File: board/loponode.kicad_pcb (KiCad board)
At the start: 2 copper layers, 44.4 x 25.9 mm, 25 parts, among them J1 DEBUG, J2 POWER_IN, J3 DBG_UART, J4 Conn_01x14, U1 TPS61322, U2 STM32L073CBTx, U3 NRF24L01+, Y1 8MHz

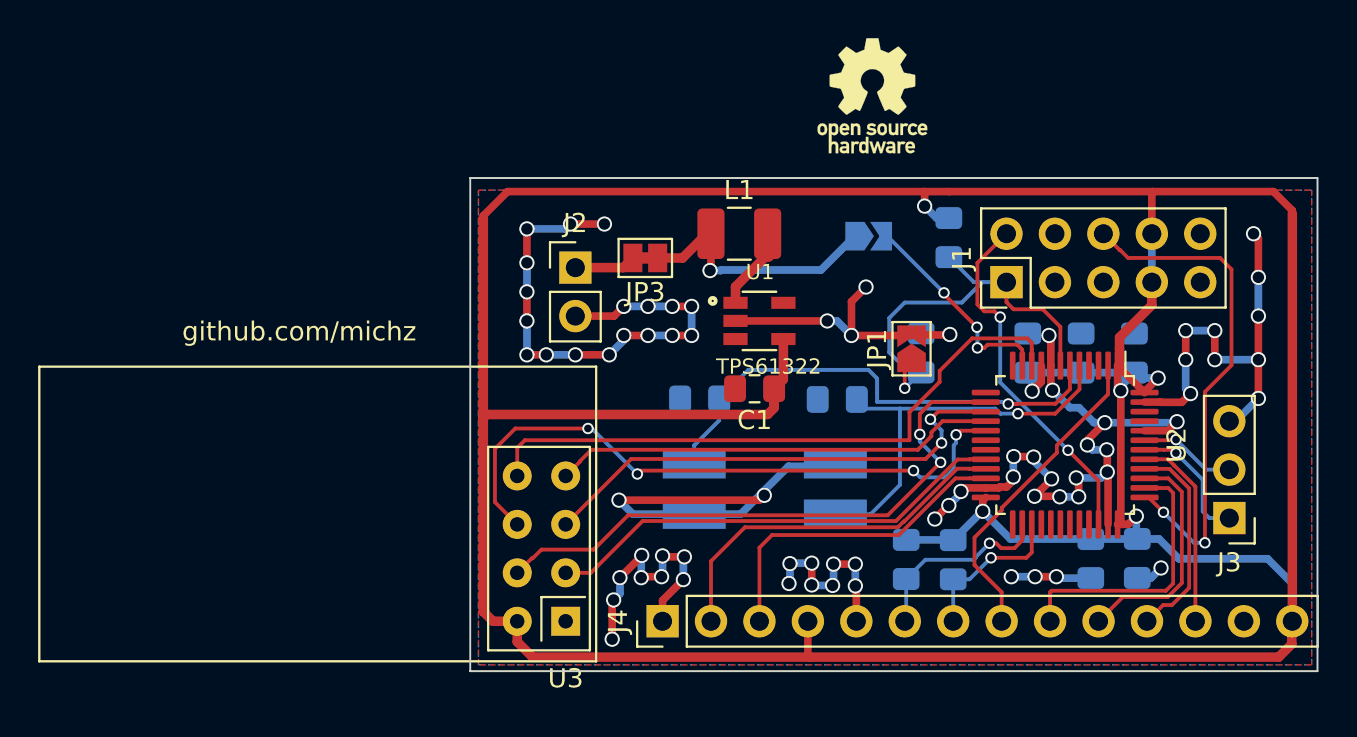
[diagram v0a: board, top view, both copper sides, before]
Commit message: move open hardware marking
+ fix some absolute path manually
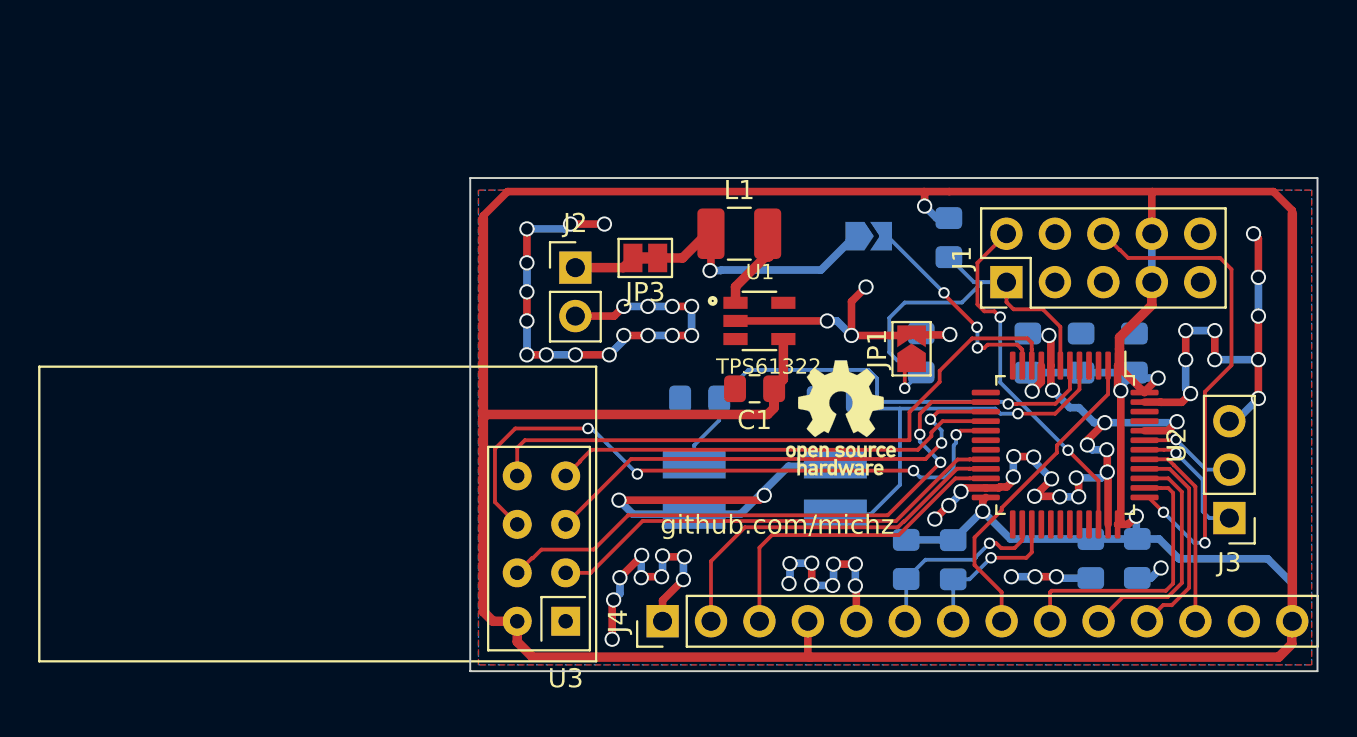
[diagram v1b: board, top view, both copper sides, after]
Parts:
- moved REF** 17.0 mm to (131.3, 134.1)
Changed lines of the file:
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@@
   )
   (module Symbol:OSHW-Logo_5.7x6mm_SilkScreen (layer F.Cu)
-    (at 132.9182 117.221)
+    (at 131.2672 134.112)
     (descr "Open Source Hardware Logo")
     (tags "Logo OSHW")
@@
   (gr_line (start 156.2608 147.3962) (end 156.2608 121.539) (layer Edge.Cuts) (width 0.1))
   (gr_line (start 111.8362 147.3962) (end 156.2608 147.3962) (layer Edge.Cuts) (width 0.1))
-  (gr_text github.com/michz (at 102.87 129.5908) (layer F.SilkS)
+  (gr_text github.com/michz (at 127.9398 139.7254) (layer F.SilkS)
     (effects (font (size 1 1) (thickness 0.15)))
   )
